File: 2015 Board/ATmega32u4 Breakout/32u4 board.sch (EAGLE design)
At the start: 16 parts, among them X1 MINI-USB-UX60A-MB-5ST

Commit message: Started to shave 100mil off the board
Started the process to see if I could shave 100mill off to show up jake.
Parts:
- C18, C19: value 20pF -> 0.1uF; device resistor:C-USC0805 -> SparkFun-Capacitors:0.1UF-25V(+80/-20%)(0603)
- C20: value 1µF -> 0.1uF; device resistor:C-USC0805 -> SparkFun-Capacitors:0.1UF-25V(+80/-20%)(0603)
- C21: value 100nF -> 0.1uF; device resistor:C-USC0805 -> SparkFun-Capacitors:0.1UF-25V(+80/-20%)(0603)
- C6: value 4.7µF -> 0.1uF; device resistor:C-USC0805 -> SparkFun-Capacitors:0.1UF-25V(+80/-20%)(0603)
- C7: value 100nF -> 1.0uF; device resistor:C-USC0805 -> SparkFun-Capacitors:1.0UF-16V-10%(0603)
- R18, R19, R23: device resistor:R-US_M0805 -> SparkFun-Passives:RESISTOR0603-RES
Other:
- moved on the sheet: C18, C19, C20, C21, C6, C7
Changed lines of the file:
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@@
 <part name="GND1" library="supply1" deviceset="GND" device=""/>
 <part name="GND5" library="supply1" deviceset="GND" device=""/>
-<part name="C7" library="resistor" deviceset="C-US" device="C0805" value="100nF"/>
-<part name="C18" library="resistor" deviceset="C-US" device="C0805" value="20pF"/>
-<part name="C19" library="resistor" deviceset="C-US" device="C0805" value="20pF"/>
+<part name="C7" library="SparkFun-Capacitors" deviceset="1.0UF-16V-10%(0603)" device="" value="1.0uF"/>
+<part name="C18" library="SparkFun-Capacitors" deviceset="0.1UF-25V(+80/-20%)(0603)" device="" value="0.1uF"/>
+<part name="C19" library="SparkFun-Capacitors" deviceset="0.1UF-25V(+80/-20%)(0603)" device="" value="0.1uF"/>
 <part name="GND30" library="supply1" deviceset="GND" device=""/>
 <part name="GND31" library="supply1" deviceset="GND" device=""/>
 <part name="U$3" library="SparkFun-DigitalIC" deviceset="ATMEGA32U4" device="TQFP-44"/>
-<part name="R18" library="resistor" deviceset="R-US_" device="M0805" value="10k"/>
+<part name="R18" library="SparkFun-Passives" deviceset="RESISTOR" device="0603-RES" value="10k"/>
 <part name="P+8" library="supply1" deviceset="VCC" device=""/>
-<part name="R19" library="resistor" deviceset="R-US_" device="M0805" value="22"/>
-<part name="R23" library="resistor" deviceset="R-US_" device="M0805" value="22"/>
-<part name="C6" library="resistor" deviceset="C-US" device="C0805" value="4.7µF"/>
+<part name="R19" library="SparkFun-Passives" deviceset="RESISTOR" device="0603-RES" value="22"/>
+<part name="R23" library="SparkFun-Passives" deviceset="RESISTOR" device="0603-RES" value="22"/>
+<part name="C6" library="SparkFun-Capacitors" deviceset="0.1UF-25V(+80/-20%)(0603)" device="" value="0.1uF"/>
 <part name="MH2029-300Y" library="resistor" deviceset="L-US" device="L2012C"/>
-<part name="C20" library="resistor" deviceset="C-US" device="C0805" value="1µF"/>
+<part name="C20" library="SparkFun-Capacitors" deviceset="0.1UF-25V(+80/-20%)(0603)" device="" value="0.1uF"/>
 <part name="GND27" library="supply1" deviceset="GND" device=""/>
-<part name="C21" library="resistor" deviceset="C-US" device="C0805" value="100nF"/>
+<part name="C21" library="SparkFun-Capacitors" deviceset="0.1UF-25V(+80/-20%)(0603)" device="" value="0.1uF"/>
 <part name="GND29" library="supply1" deviceset="GND" device=""/>
 <part name="P+6" library="supply1" deviceset="VCC" device=""/>
@@
 <pinref part="U$3" gate="G$1" pin="UGND"/>
 <wire x1="208.28" y1="144.78" x2="200.66" y2="144.78" width="0.1524" layer="91"/>
-<wire x1="200.66" y1="144.78" x2="200.66" y2="147.32" width="0.1524" layer="91"/>
 <pinref part="C6" gate="G$1" pin="2"/>
 <junction x="200.66" y="142.24"/>
 <wire x1="200.66" y1="142.24" x2="200.66" y2="144.78" width="0.1524" layer="91"/>
 <junction x="200.66" y="144.78"/>
-<wire x1="200.66" y1="144.78" x2="200.66" y2="147.32" width="0.1524" layer="91"/>
-<junction x="200.66" y="147.32"/>
+<wire x1="200.66" y1="144.78" x2="200.66" y2="149.86" width="0.1524" layer="91"/>
+<junction x="200.66" y="149.86"/>
 </segment>
 <segment>
@@
 <wire x1="269.24" y1="2.54" x2="266.7" y2="2.54" width="0.1524" layer="91"/>
 <wire x1="266.7" y1="2.54" x2="261.62" y2="2.54" width="0.1524" layer="91"/>
-<wire x1="261.62" y1="2.54" x2="261.62" y2="5.08" width="0.1524" layer="91"/>
+<wire x1="261.62" y1="2.54" x2="261.62" y2="7.62" width="0.1524" layer="91"/>
 <pinref part="C7" gate="G$1" pin="2"/>
 <pinref part="GND5" gate="1" pin="GND"/>
@@
 <pinref part="C18" gate="G$1" pin="2"/>
 <pinref part="GND30" gate="1" pin="GND"/>
-<wire x1="162.56" y1="144.78" x2="162.56" y2="147.32" width="0.1524" layer="91"/>
+<wire x1="162.56" y1="144.78" x2="162.56" y2="149.86" width="0.1524" layer="91"/>
 </segment>
 <segment>
 <pinref part="C19" gate="G$1" pin="2"/>
 <pinref part="GND31" gate="1" pin="GND"/>
-<wire x1="152.4" y1="144.78" x2="152.4" y2="147.32" width="0.1524" layer="91"/>
+<wire x1="152.4" y1="144.78" x2="152.4" y2="149.86" width="0.1524" layer="91"/>
 </segment>
 <segment>
@@
 <wire x1="180.34" y1="190.5" x2="180.34" y2="195.58" width="0.1524" layer="91"/>
 <wire x1="180.34" y1="195.58" x2="180.34" y2="203.2" width="0.1524" layer="91"/>
-<wire x1="180.34" y1="203.2" x2="182.88" y2="203.2" width="0.1524" layer="91"/>
+<wire x1="180.34" y1="203.2" x2="185.42" y2="203.2" width="0.1524" layer="91"/>
 <pinref part="C20" gate="G$1" pin="2"/>
 <pinref part="C21" gate="G$1" pin="2"/>
-<wire x1="182.88" y1="195.58" x2="180.34" y2="195.58" width="0.1524" layer="91"/>
+<wire x1="185.42" y1="195.58" x2="180.34" y2="195.58" width="0.1524" layer="91"/>
 <junction x="180.34" y="195.58"/>
 </segment>
@@
 <segment>
 <pinref part="C19" gate="G$1" pin="1"/>
-<wire x1="152.4" y1="154.94" x2="152.4" y2="162.56" width="0.1524" layer="91"/>
+<wire x1="152.4" y1="157.48" x2="152.4" y2="162.56" width="0.1524" layer="91"/>
 <wire x1="208.28" y1="162.56" x2="182.88" y2="162.56" width="0.1524" layer="91"/>
 <pinref part="U$3" gate="G$1" pin="XTAL1"/>
@@
 <segment>
 <pinref part="C18" gate="G$1" pin="1"/>
-<wire x1="162.56" y1="157.48" x2="162.56" y2="154.94" width="0.1524" layer="91"/>
 <pinref part="U$3" gate="G$1" pin="XTAL2"/>
 <wire x1="162.56" y1="157.48" x2="182.88" y2="157.48" width="0.1524" layer="91"/>
@@
 <wire x1="208.28" y1="195.58" x2="195.58" y2="195.58" width="0.1524" layer="91"/>
 <pinref part="C21" gate="G$1" pin="1"/>
-<wire x1="195.58" y1="195.58" x2="190.5" y2="195.58" width="0.1524" layer="91"/>
+<wire x1="195.58" y1="195.58" x2="193.04" y2="195.58" width="0.1524" layer="91"/>
 <wire x1="195.58" y1="195.58" x2="195.58" y2="187.96" width="0.1524" layer="91"/>
 <wire x1="195.58" y1="187.96" x2="193.04" y2="187.96" width="0.1524" layer="91"/>
@@
 <pinref part="U$3" gate="G$1" pin="UCAP"/>
 <wire x1="208.28" y1="180.34" x2="200.66" y2="180.34" width="0.1524" layer="91"/>
-<wire x1="200.66" y1="180.34" x2="200.66" y2="154.94" width="0.1524" layer="91"/>
+<wire x1="200.66" y1="180.34" x2="200.66" y2="157.48" width="0.1524" layer="91"/>
 <pinref part="C6" gate="G$1" pin="1"/>
 </segment>
@@
 <wire x1="193.04" y1="205.74" x2="193.04" y2="203.2" width="0.1524" layer="91"/>
 <pinref part="C20" gate="G$1" pin="1"/>
-<wire x1="193.04" y1="203.2" x2="190.5" y2="203.2" width="0.1524" layer="91"/>
 <wire x1="203.2" y1="200.66" x2="193.04" y2="200.66" width="0.1524" layer="91"/>
 <wire x1="193.04" y1="200.66" x2="193.04" y2="203.2" width="0.1524" layer="91"/>
@@
 <net name="VBUS" class="0">
 <segment>
-<wire x1="261.62" y1="20.32" x2="261.62" y2="12.7" width="0.1524" layer="91"/>
+<wire x1="261.62" y1="20.32" x2="261.62" y2="15.24" width="0.1524" layer="91"/>
 <pinref part="C7" gate="G$1" pin="1"/>
 <label x="248.92" y="20.32" size="1.27" layer="95" rot="R180" xref="yes"/>

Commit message: Added a reset button
Reset button to the board so we can reset it easily.
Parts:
- added S1: SWITCH-MOMENTARY-2SMD, SparkFun-Electromechanical:SWITCH-MOMENTARY-2SMD
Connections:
- net GND: now also S1.1
- net RST: now also S1.2
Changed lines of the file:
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@@
 <part name="JP2" library="pinhead" deviceset="PINHD-1X16" device=""/>
 <part name="GND2" library="supply1" deviceset="GND" device=""/>
+<part name="S1" library="SparkFun-Electromechanical" deviceset="SWITCH-MOMENTARY-2" device="SMD"/>
+<part name="GND3" library="supply1" deviceset="GND" device=""/>
 </parts>
 <sheets>
@@
 <instance part="JP2" gate="A" x="312.42" y="231.14"/>
 <instance part="GND2" gate="1" x="299.72" y="154.94"/>
+<instance part="S1" gate="G$1" x="208.28" y="259.08"/>
+<instance part="GND3" gate="1" x="198.12" y="259.08" rot="R270"/>
 </instances>
 <busses>
@@
 <label x="302.26" y="246.38" size="1.27" layer="95" rot="R180" xref="yes"/>
 </segment>
+<segment>
+<pinref part="S1" gate="G$1" pin="1"/>
+<pinref part="GND3" gate="1" pin="GND"/>
+<wire x1="200.66" y1="259.08" x2="203.2" y2="259.08" width="0.1524" layer="91"/>
+</segment>
 </net>
 <net name="D+" class="0">
@@
 <wire x1="208.28" y1="208.28" x2="205.74" y2="208.28" width="0.1524" layer="91"/>
 <wire x1="205.74" y1="208.28" x2="205.74" y2="215.9" width="0.1524" layer="91"/>
-<wire x1="215.9" y1="226.06" x2="215.9" y2="241.3" width="0.1524" layer="91"/>
 <junction x="215.9" y="226.06"/>
 <wire x1="205.74" y1="215.9" x2="215.9" y2="215.9" width="0.1524" layer="91"/>
@@
 <wire x1="215.9" y1="226.06" x2="210.82" y2="226.06" width="0.1524" layer="91"/>
 <label x="215.9" y="241.3" size="1.27" layer="95" xref="yes"/>
-</segment>
-<segment>
+<pinref part="S1" gate="G$1" pin="2"/>
+<wire x1="213.36" y1="259.08" x2="215.9" y2="259.08" width="0.1524" layer="91"/>
+<wire x1="215.9" y1="259.08" x2="215.9" y2="226.06" width="0.1524" layer="91"/>
+</segment>
+<segment>

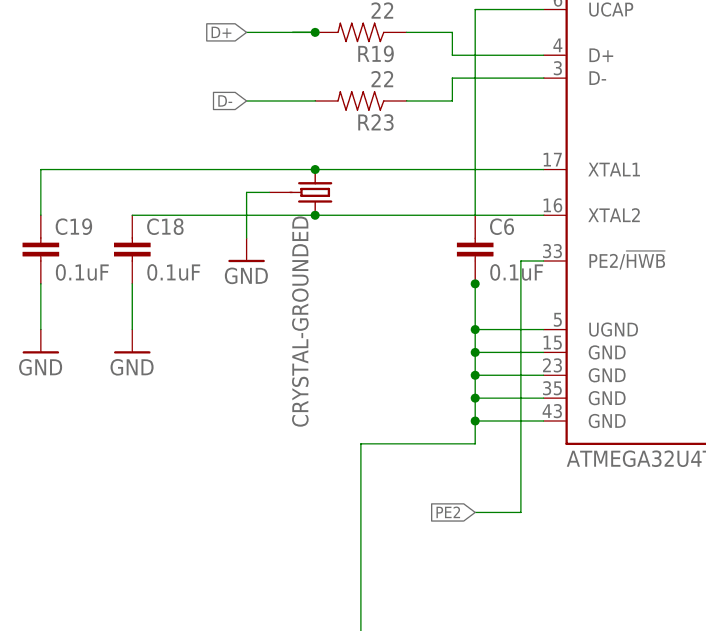
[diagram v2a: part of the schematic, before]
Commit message: Replaced crystal with resonator
Resonator instead crystal and caps to save space and cut down on number
of parts to cut cost.
Resonator Part #CSTCE16M0V53-R0
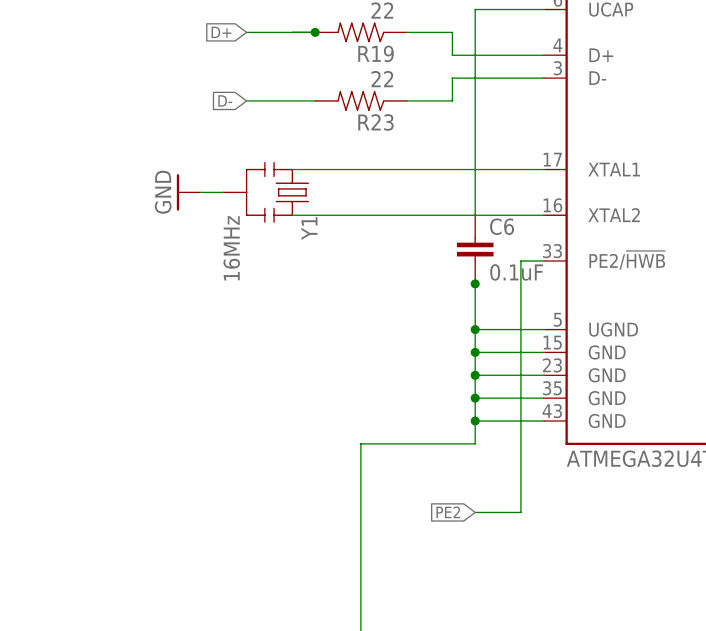
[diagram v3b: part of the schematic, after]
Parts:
- removed C18, C19: 0.1uF, SparkFun-Capacitors:0.1UF-25V(+80/-20%)(0603)
- removed U$4: CRYSTAL-GROUNDED, SparkFun-FreqCtrl:CRYSTAL-GROUNDED
- added Y1: 16MHz, SparkFun-FreqCtrl:RESONATOR16MHZ
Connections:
- net GND: now also Y1.2; no longer C18.2, C19.2, U$4.3
- net N$39: now also Y1.1; no longer C19.1, U$4.1
- net N$41: now also Y1.3; no longer C18.1, U$4.2
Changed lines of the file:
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@@
 <part name="GND5" library="supply1" deviceset="GND" device=""/>
 <part name="C7" library="SparkFun-Capacitors" deviceset="1.0UF-16V-10%(0603)" device="" value="1.0uF"/>
-<part name="C18" library="SparkFun-Capacitors" deviceset="0.1UF-25V(+80/-20%)(0603)" device="" value="0.1uF"/>
-<part name="C19" library="SparkFun-Capacitors" deviceset="0.1UF-25V(+80/-20%)(0603)" device="" value="0.1uF"/>
-<part name="GND30" library="supply1" deviceset="GND" device=""/>
-<part name="GND31" library="supply1" deviceset="GND" device=""/>
 <part name="U$3" library="SparkFun-DigitalIC" deviceset="ATMEGA32U4" device="TQFP-44"/>
 <part name="R18" library="SparkFun-Passives" deviceset="RESISTOR" device="0603-RES" value="10k"/>
@@
 <part name="P+6" library="supply1" deviceset="VCC" device=""/>
 <part name="U$2" library="Jake" deviceset="ICSP_SMD" device=""/>
-<part name="U$4" library="SparkFun-FreqCtrl" deviceset="CRYSTAL-GROUNDED" device=""/>
-<part name="GND26" library="supply1" deviceset="GND" device=""/>
 <part name="X1" library="con-hirose" deviceset="MINI-USB-" device="UX60A-MB-5ST"/>
 <part name="JP1" library="pinhead" deviceset="PINHD-1X16" device=""/>
@@
 <part name="S1" library="SparkFun-Electromechanical" deviceset="SWITCH-MOMENTARY-2" device="SMD"/>
 <part name="GND3" library="supply1" deviceset="GND" device=""/>
+<part name="Y1" library="SparkFun-FreqCtrl" deviceset="RESONATOR" device="16MHZ" value="16MHz"/>
+<part name="GND4" library="supply1" deviceset="GND" device=""/>
 </parts>
 <sheets>
@@
 <instance part="GND5" gate="1" x="266.7" y="-2.54"/>
 <instance part="C7" gate="G$1" x="261.62" y="10.16"/>
-<instance part="C18" gate="G$1" x="162.56" y="152.4"/>
-<instance part="C19" gate="G$1" x="152.4" y="152.4"/>
-<instance part="GND30" gate="1" x="162.56" y="142.24"/>
-<instance part="GND31" gate="1" x="152.4" y="142.24"/>
 <instance part="U$3" gate="G$1" x="226.06" y="172.72"/>
 <instance part="R18" gate="G$1" x="205.74" y="226.06" rot="R180"/>
@@
 <instance part="P+6" gate="VCC" x="251.46" y="48.26"/>
 <instance part="U$2" gate="G$1" x="279.4" y="33.02"/>
-<instance part="U$4" gate="G$1" x="182.88" y="160.02" rot="R270"/>
-<instance part="GND26" gate="1" x="175.26" y="152.4"/>
 <instance part="X1" gate="G$1" x="281.94" y="15.24"/>
 <instance part="JP1" gate="A" x="312.42" y="177.8"/>
@@
 <instance part="S1" gate="G$1" x="208.28" y="259.08"/>
 <instance part="GND3" gate="1" x="198.12" y="259.08" rot="R270"/>
+<instance part="Y1" gate="G$1" x="180.34" y="160.02" rot="R270"/>
+<instance part="GND4" gate="1" x="167.64" y="160.02" rot="R270"/>
 </instances>
 <busses>
@@
 </segment>
 <segment>
-<pinref part="C18" gate="G$1" pin="2"/>
-<pinref part="GND30" gate="1" pin="GND"/>
-<wire x1="162.56" y1="144.78" x2="162.56" y2="149.86" width="0.1524" layer="91"/>
-</segment>
-<segment>
-<pinref part="C19" gate="G$1" pin="2"/>
-<pinref part="GND31" gate="1" pin="GND"/>
-<wire x1="152.4" y1="144.78" x2="152.4" y2="149.86" width="0.1524" layer="91"/>
-</segment>
-<segment>
 <pinref part="GND27" gate="1" pin="GND"/>
 <wire x1="180.34" y1="190.5" x2="180.34" y2="195.58" width="0.1524" layer="91"/>
@@
 </segment>
 <segment>
-<pinref part="U$4" gate="G$1" pin="3"/>
-<pinref part="GND26" gate="1" pin="GND"/>
-<wire x1="175.26" y1="154.94" x2="175.26" y2="160.02" width="0.1524" layer="91"/>
-<wire x1="175.26" y1="160.02" x2="177.8" y2="160.02" width="0.1524" layer="91"/>
-</segment>
-<segment>
 <pinref part="JP1" gate="A" pin="16"/>
 <wire x1="309.88" y1="157.48" x2="299.72" y2="157.48" width="0.1524" layer="91"/>
@@
 <pinref part="GND3" gate="1" pin="GND"/>
 <wire x1="200.66" y1="259.08" x2="203.2" y2="259.08" width="0.1524" layer="91"/>
+</segment>
+<segment>
+<pinref part="Y1" gate="G$1" pin="2"/>
+<pinref part="GND4" gate="1" pin="GND"/>
+<wire x1="170.18" y1="160.02" x2="172.72" y2="160.02" width="0.1524" layer="91"/>
 </segment>
 </net>
@@
 <net name="N$39" class="0">
 <segment>
-<pinref part="C19" gate="G$1" pin="1"/>
-<wire x1="152.4" y1="157.48" x2="152.4" y2="162.56" width="0.1524" layer="91"/>
-<wire x1="208.28" y1="162.56" x2="182.88" y2="162.56" width="0.1524" layer="91"/>
+<wire x1="208.28" y1="162.56" x2="180.34" y2="162.56" width="0.1524" layer="91"/>
 <pinref part="U$3" gate="G$1" pin="XTAL1"/>
-<pinref part="U$4" gate="G$1" pin="1"/>
-<wire x1="182.88" y1="162.56" x2="152.4" y2="162.56" width="0.1524" layer="91"/>
-<junction x="182.88" y="162.56"/>
+<pinref part="Y1" gate="G$1" pin="1"/>
 </segment>
 </net>
 <net name="N$41" class="0">
 <segment>
-<pinref part="C18" gate="G$1" pin="1"/>
 <pinref part="U$3" gate="G$1" pin="XTAL2"/>
-<wire x1="162.56" y1="157.48" x2="182.88" y2="157.48" width="0.1524" layer="91"/>
-<pinref part="U$4" gate="G$1" pin="2"/>
-<wire x1="182.88" y1="157.48" x2="208.28" y2="157.48" width="0.1524" layer="91"/>
-<junction x="182.88" y="157.48"/>
+<wire x1="180.34" y1="157.48" x2="208.28" y2="157.48" width="0.1524" layer="91"/>
+<pinref part="Y1" gate="G$1" pin="3"/>
 </segment>
 </net>
